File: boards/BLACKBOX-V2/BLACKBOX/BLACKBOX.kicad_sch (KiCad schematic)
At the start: 25 parts, among them J1 Micro_SD_Card, J101 Conn_01x08_Female, J102 Conn_01x02_Female, J3 Conn_01x02_Female, U1 Adafruit-BNO085, U2 KX122-1042, U3 MS5611-01BA

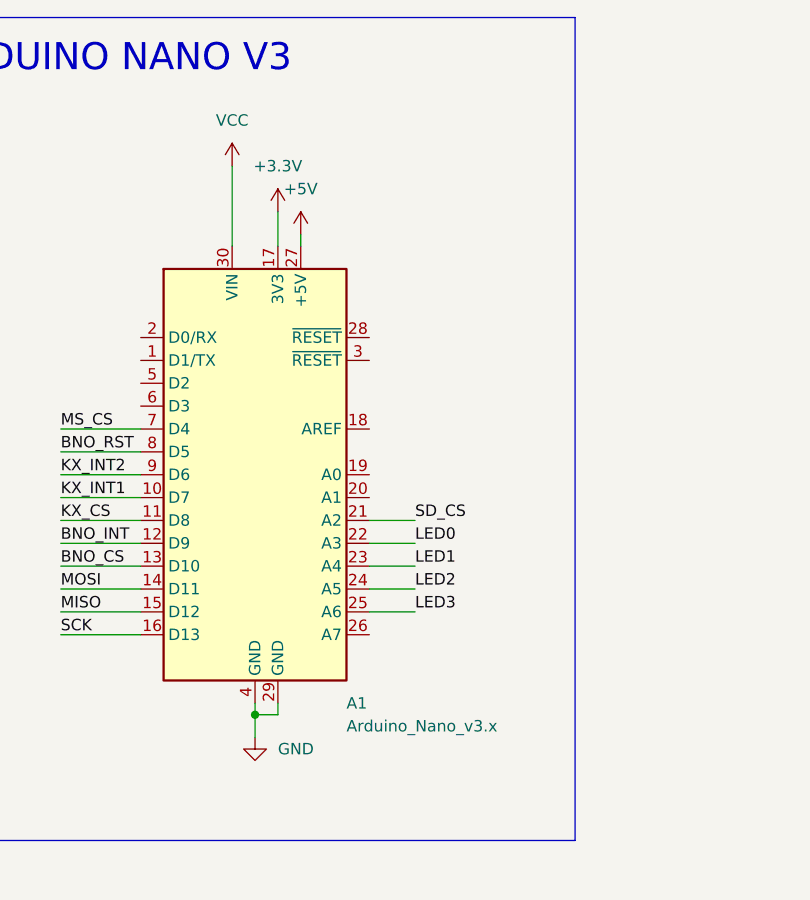
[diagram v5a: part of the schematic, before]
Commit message: added switch to blackbox;
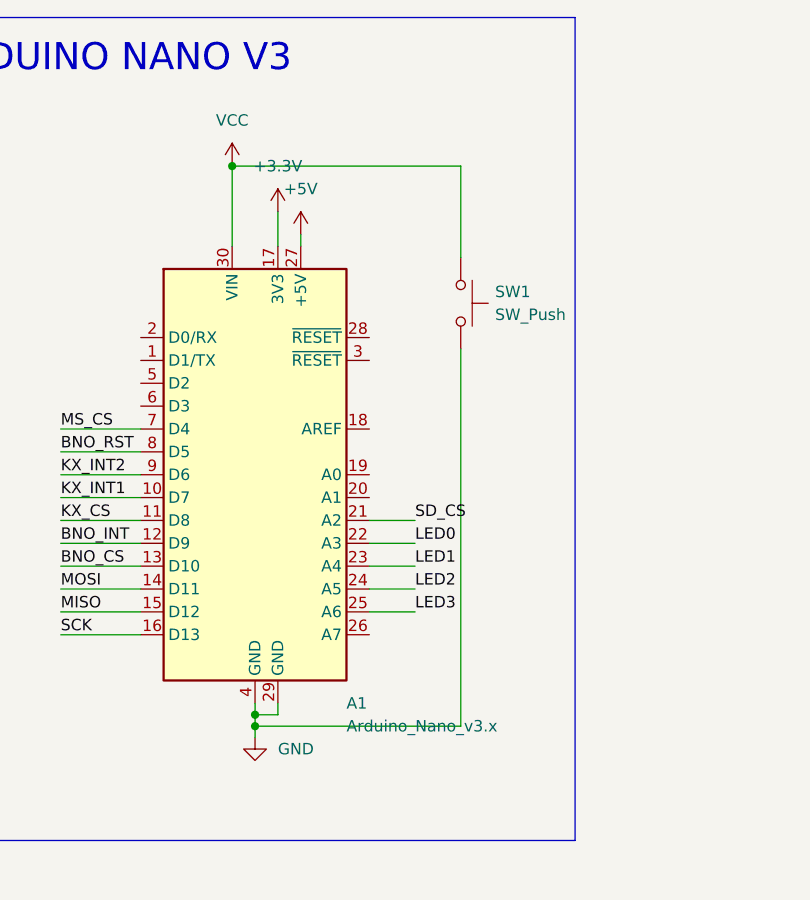
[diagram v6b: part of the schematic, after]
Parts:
- added SW1: SW_Push, Button_Switch_SMD:SW_SPST_FSMSM, symbol Switch:SW_Push
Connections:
- net GND: now also SW1.2
- net VCC: now also SW1.1
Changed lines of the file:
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@@
   (junction (at 31.75 93.98) (diameter 0) (color 0 0 0 0)
   )
+  (junction (at 153.67 91.44) (diameter 0) (color 0 0 0 0)
+  )
   (junction (at 261.239 35.941) (diameter 0) (color 0 0 0 0)
   )
@@
   )
   (junction (at 70.485 32.385) (diameter 0) (color 0 0 0 0)
+  )
+  (junction (at 151.13 29.21) (diameter 0) (color 0 0 0 0)
   )
   (no_connect (at 80.645 53.34))
@@
     (stroke (width 0) (type default) (color 0 0 0 0))
   )
-  (wire (pts (xy 153.67 92.71) (xy 153.67 90.17))
+  (wire (pts (xy 153.67 92.71) (xy 153.67 91.44))
     (stroke (width 0) (type default) (color 0 0 0 0))
   )
@@
     (stroke (width 0) (type default) (color 0 0 0 0))
   )
+  (wire (pts (xy 153.67 91.44) (xy 153.67 90.17))
+    (stroke (width 0) (type default) (color 0 0 0 0))
+  )
   (polyline (pts (xy 19.685 139.065) (xy 19.685 189.865))
     (stroke (width 0) (type default) (color 0 0 0 0))
@@
     (stroke (width 0) (type default) (color 0 0 0 0))
   )
+  (wire (pts (xy 176.53 29.21) (xy 176.53 39.37))
+    (stroke (width 0) (type default) (color 0 0 0 0))
+  )
   (polyline (pts (xy 189.23 104.14) (xy 116.84 104.14))
     (stroke (width 0) (type default) (color 0 0 0 0))
@@
     (stroke (width 0) (type default) (color 0 0 0 0))
   )
+  (wire (pts (xy 151.13 29.21) (xy 176.53 29.21))
+    (stroke (width 0) (type default) (color 0 0 0 0))
+  )
   (wire (pts (xy 71.12 161.29) (xy 77.47 161.29))
     (stroke (width 0) (type default) (color 0 0 0 0))
@@
     (stroke (width 0) (type default) (color 0 0 0 0))
   )
+  (wire (pts (xy 176.53 49.53) (xy 176.53 91.44))
+    (stroke (width 0) (type default) (color 0 0 0 0))
+  )
   (polyline (pts (xy 104.775 73.025) (xy 20.32 73.025))
     (stroke (width 0) (type default) (color 0 0 0 0))
@@
   )
   (wire (pts (xy 224.155 79.375) (xy 224.155 86.995))
+    (stroke (width 0) (type default) (color 0 0 0 0))
+  )
+  (wire (pts (xy 176.53 91.44) (xy 153.67 91.44))
     (stroke (width 0) (type default) (color 0 0 0 0))
   )
@@
     (pin "1")
   )
+  (symbol (lib_id "Switch:SW_Push") (at 176.53 44.45 270) (unit 1)
+    (in_bom yes) (on_board yes) (fields_autoplaced)
+    (property "Reference" "SW1" (id 0) (at 180.34 43.1799 90)
+      (effects (font (size 1.27 1.27)) (justify left))
+    )
+    (property "Value" "SW_Push" (id 1) (at 180.34 45.7199 90)
+      (effects (font (size 1.27 1.27)) (justify left))
+    )
+    (property "Footprint" "Button_Switch_SMD:SW_SPST_FSMSM" (id 2) (at 181.61 44.45 0)
+      (effects (font (size 1.27 1.27)) hide)
+    )
+    (property "Datasheet" "~" (id 3) (at 181.61 44.45 0)
+      (effects (font (size 1.27 1.27)) hide)
+    )
+    (pin "1")
+    (pin "2")
+  )
   (symbol (lib_id "Device:Jumper_NC_Small") (at 57.785 32.385 0) (unit 1)
     (in_bom yes) (on_board yes)
@@
       (reference "R6") (unit 1) (value "10k") (footprint "Resistor_SMD:R_0805_2012Metric")
     )
+    (path "/2f853f46-8ebf-4396-9087-6b1faf341779"
+      (reference "SW1") (unit 1) (value "SW_Push") (footprint "Button_Switch_SMD:SW_SPST_FSMSM")
+    )
     (path "/404f94fb-b5b6-4fb6-ab7d-efc1587752a4"

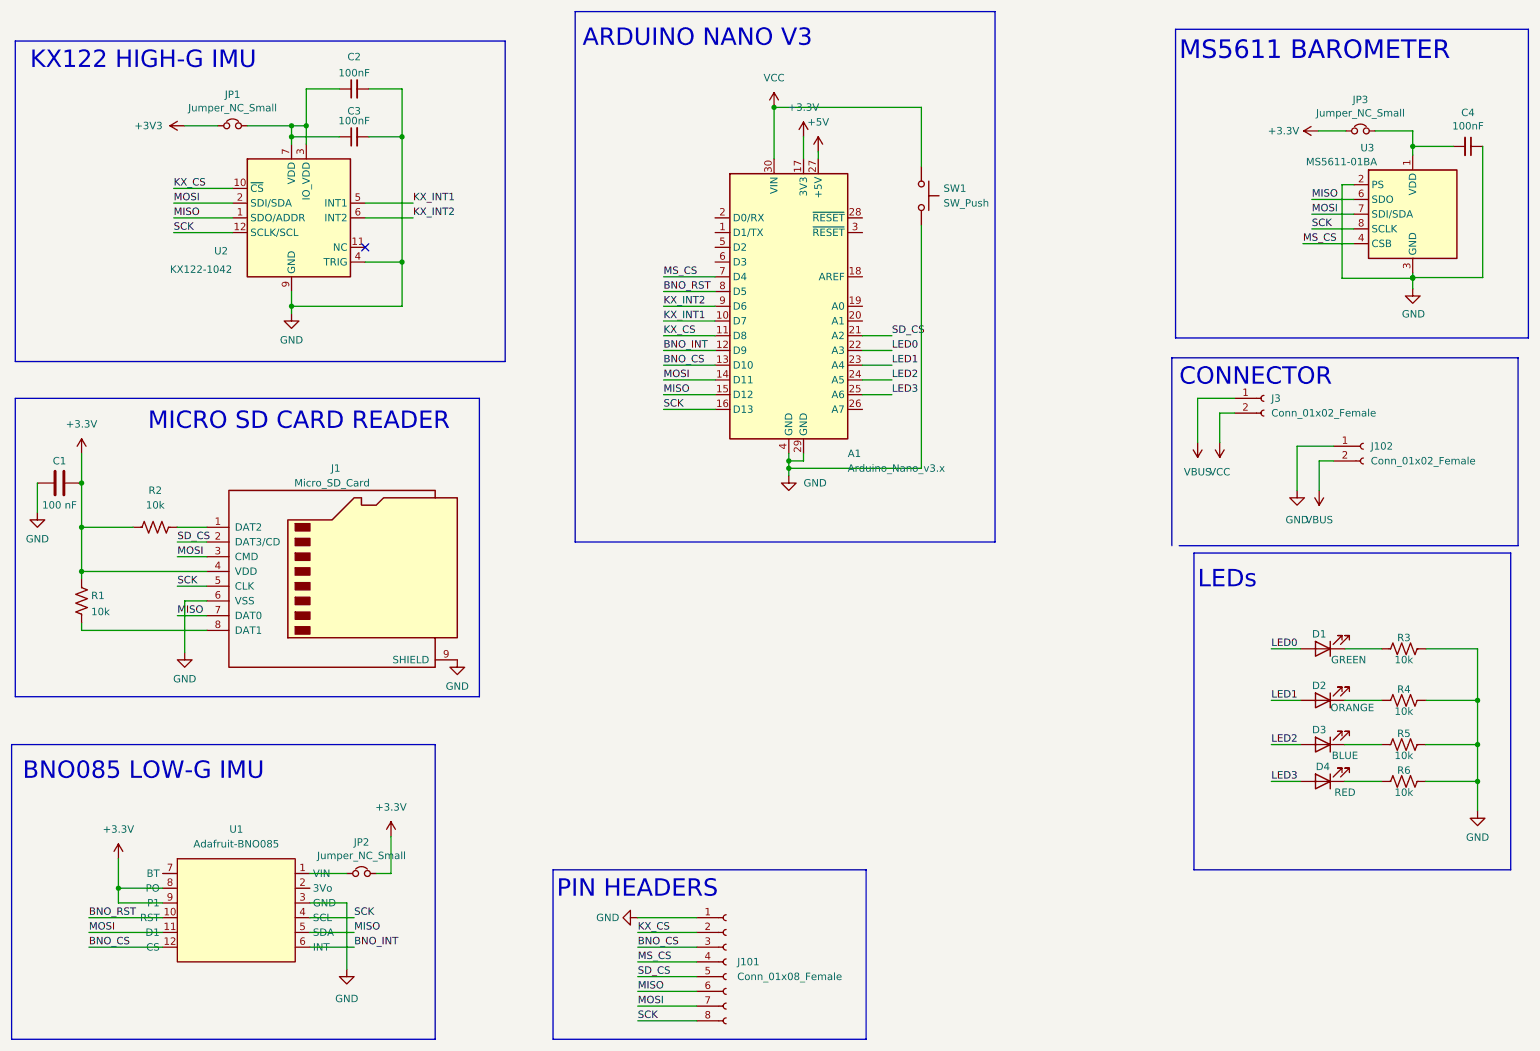
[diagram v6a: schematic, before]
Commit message: Fixed BNO symbol and a few suspect traces
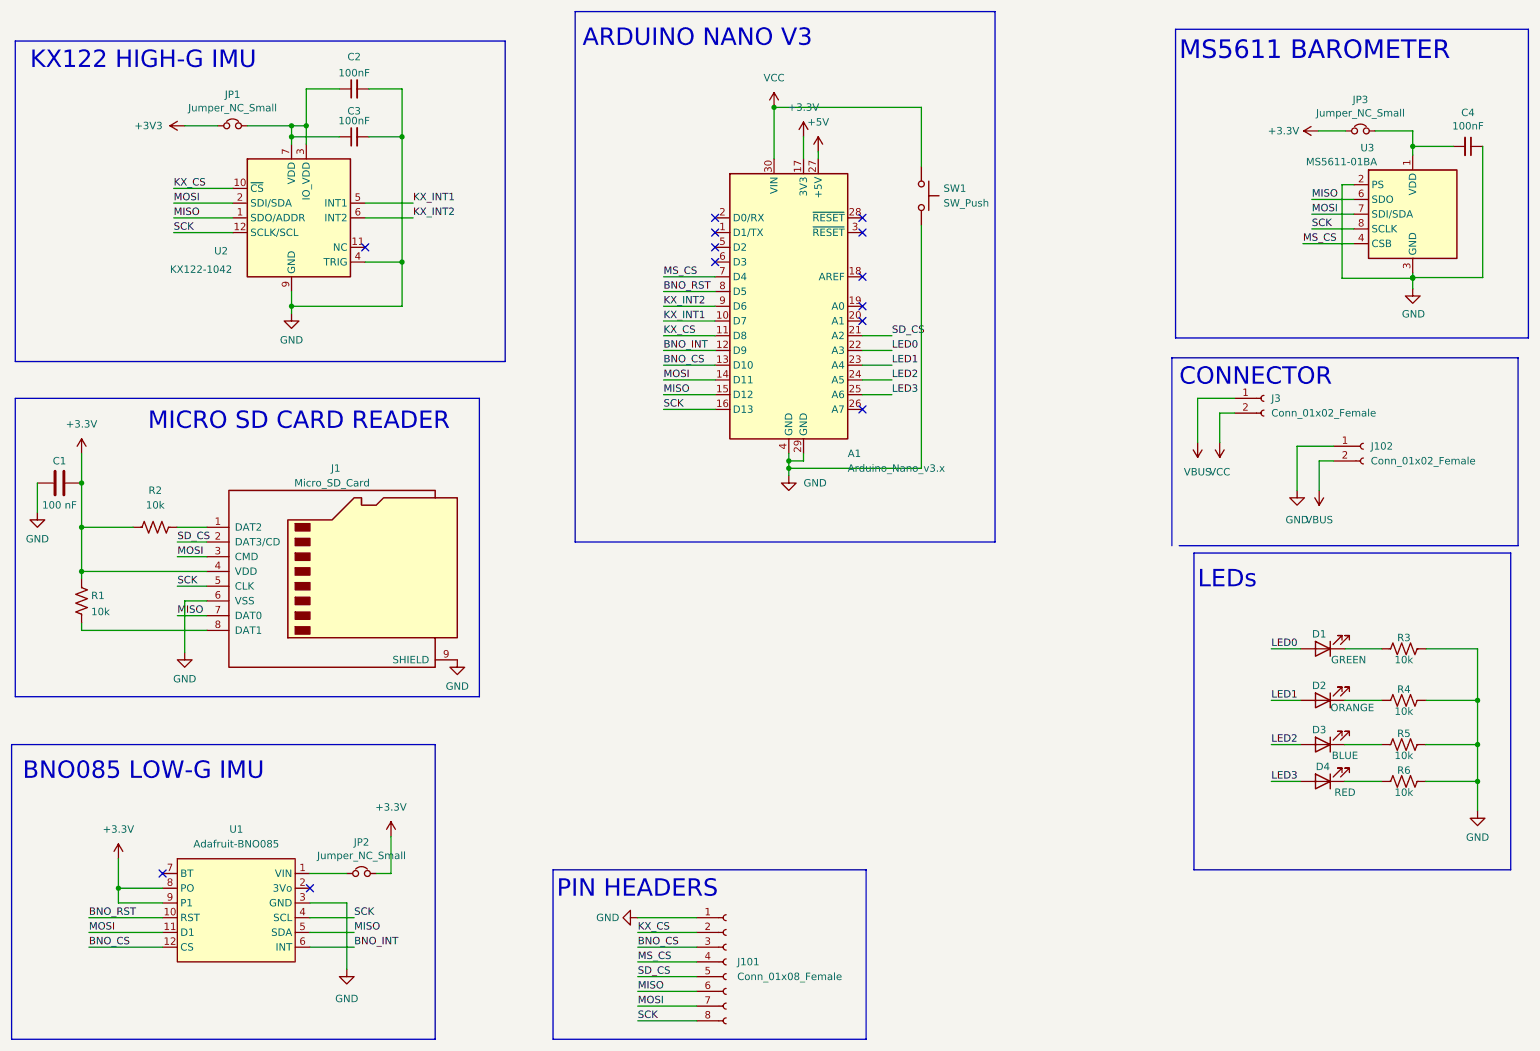
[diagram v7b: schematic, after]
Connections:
- net +3V3: now also U1.8 (PO), U1.9 (P1)
- net BNO_CS: now also U1.12 (CS)
- net BNO_INT: now also U1.6 (INT)
- net BNO_RST: now also U1.10 (RST)
- net GND: now also U1.3 (GND)
- net MISO: now also U1.5 (SDA)
- net MOSI: now also U1.11 (D1)
- net SCK: now also U1.4 (SCL)
- net at U1.1 (VIN): now also JP2.1
- no-connect marks 1 -> 13
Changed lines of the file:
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@@
   )
   (no_connect (at 80.645 53.34))
+  (no_connect (at 45.72 161.29))
+  (no_connect (at 71.12 163.83))
+  (no_connect (at 166.37 58.42))
+  (no_connect (at 166.37 50.8))
+  (no_connect (at 166.37 48.26))
+  (no_connect (at 166.37 63.5))
+  (no_connect (at 166.37 66.04))
+  (no_connect (at 166.37 81.28))
+  (no_connect (at 140.97 53.34))
+  (no_connect (at 140.97 50.8))
+  (no_connect (at 140.97 55.88))
+  (no_connect (at 140.97 48.26))
   (wire (pts (xy 132.08 63.5) (xy 140.97 63.5))
     (stroke (width 0) (type default) (color 0 0 0 0))
